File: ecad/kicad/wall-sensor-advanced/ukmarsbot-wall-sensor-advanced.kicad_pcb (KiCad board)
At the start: 2 copper layers, 27.3 x 80 mm, 30 parts, among them J1 Conn_01x14, Q1 TEFT4300, Q2 TEFT4300, Q3 TEFT4300, Q4 TEFT4300, Q5 BC337, Q6 BC337

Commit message: second draft wall sensor advanced
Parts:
- added C2: 330uF, 16V, Capacitor_THT:CP_Radial_D7.5mm_P2.50mm, F.Cu at (157.1, 129.8)
- moved C1 25.2 mm to (157.1, 80.2)
- moved D5 24.4 mm to (162.2, 106.3), turned to 90 degrees
- moved R12 20.0 mm to (158.3, 101.2), turned to -90 degrees
- moved R11 6.53 mm to (153.9, 86.6), turned to 180 degrees
- moved R1 2.92 mm to (146.3, 89.5)
- moved R4 2.92 mm to (146.3, 98.8)
- moved R5 2.92 mm to (146.3, 101.8)
- moved R6 2.92 mm to (146.3, 104.9)
- moved R7 2.92 mm to (146.3, 107.9)
- moved R13 2.92 mm to (146.3, 114.0)
- moved R14 2.92 mm to (146.3, 117.1)
- moved R2 2.92 mm to (146.3, 92.7)
- moved R3 2.92 mm to (146.3, 95.7)
- moved R8 2.92 mm to (146.3, 111.0)
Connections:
- net Net-(D1-Pad1) renamed /FWD_COMMON
- net Net-(D2-Pad1) renamed /DIA_COMMON
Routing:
- net D6_LED: track 0.00 -> 51.6 mm, vias 0 -> 4
- net A0_LF: track 5.18 -> 49.4 mm
- net A3_LF: track 4.55 -> 37.8 mm
- net A1_RD: track 4.97 -> 35.5 mm, vias 0 -> 1
- net Net-(D3-Pad2): track 0.00 -> 30.2 mm
- net A2_LD: track 4.76 -> 32.3 mm, vias 0 -> 1
- net Net-(D5-Pad2): track 20.8 -> 4.86 mm
- net 5V: track 136.8 -> 152.1 mm
- net Net-(D2-Pad2): track 0.00 -> 11.7 mm, vias 0 -> 1
- net /FWD_COMMON: track 120.8 -> 109.7 mm, vias 0 -> 1
- net V_LED: track 28.6 -> 20.0 mm
- net Net-(D4-Pad2): track 41.8 -> 38.4 mm
- net Net-(Q5-Pad2): track 32.9 -> 34.9 mm, vias 0 -> 2
- net D12_DIAGONAL: track 5.60 -> 7.56 mm
- net D11_FRONT: track 5.39 -> 7.05 mm
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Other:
- rule pad_to_mask_clearance: 0.0508 -> 0

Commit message: Update Advanced Wall Sensor
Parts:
- C1, C2: footprint Capacitor_THT:CP_Radial_D7.5mm_P2.50mm -> Capacitor_THT:CP_Radial_D10.0mm_P2.50mm
- D1, D2, D3, D4: footprint LED_THT:LED_D5.0mm_Horizontal_O3.81mm_Z3.0mm -> ukmarsbot:LED_D5.0mm_Horizontal_O6.35mm_Z3.0mm
- J1: footprint Connector_PinSocket_2.54mm:PinSocket_1x14_P2.54mm_Vertical -> ukmarsbot:PinHeader_1x14_P2.54mm_Vertical_Longpads
- Q1, Q2, Q3, Q4: footprint LED_THT:LED_D5.0mm_Horizontal_O1.27mm_Z3.0mm_IRGrey -> ukmarsbot:LED_D5.0mm_Horizontal_O1.27mm_Z3.0mm_IRGrey
- moved D4 2.07 mm to (143.8, 137.9)
- moved Q4 2.07 mm to (147.8, 136.0)
- moved D1 2.02 mm to (144.3, 74.6)
- moved Q1 2.02 mm to (147.4, 71.5)
- moved R1 0.13 mm to (146.3, 89.6)
- renumbered REF** to locked
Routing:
- net D6_LED: track 51.6 -> 21.4 mm, vias 4 -> 2
- net /FWD_COMMON: track 109.7 -> 128.5 mm
- net A0_LF: track 49.4 -> 47.6 mm
- net Net-(D4-Pad2): track 38.4 -> 39.3 mm
- net A1_RD: track 35.5 -> 35.0 mm

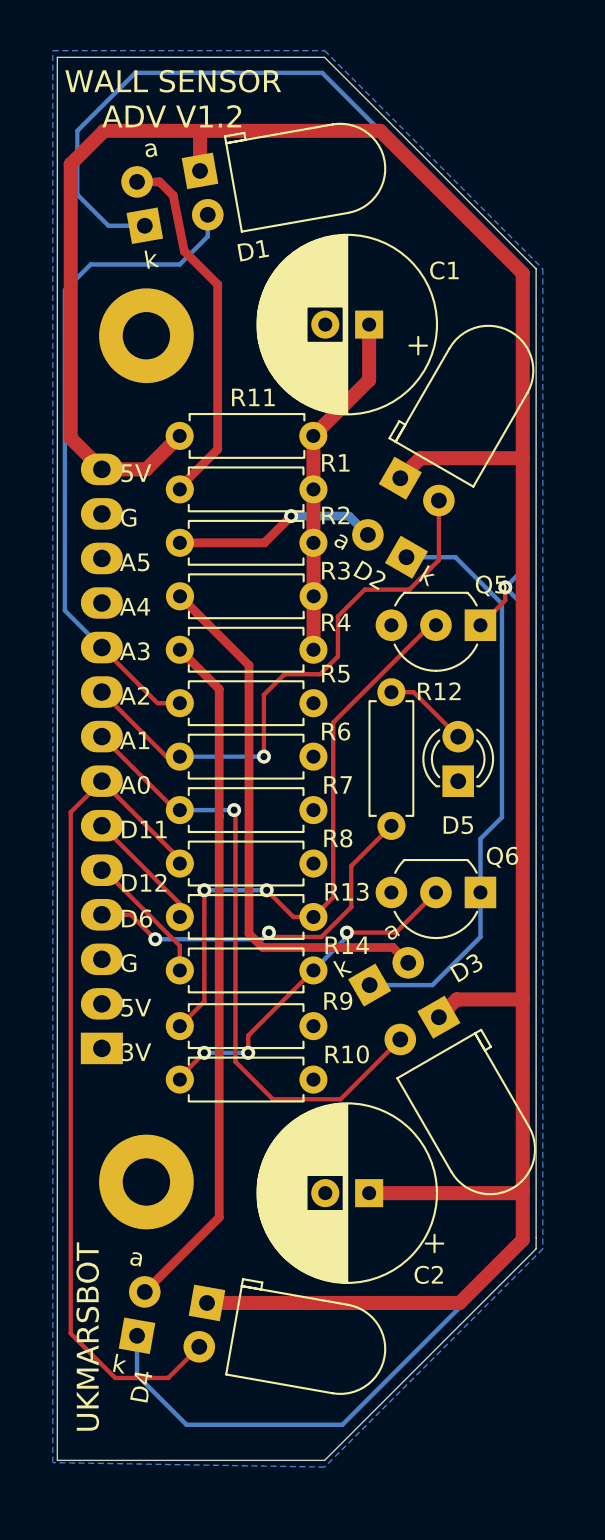
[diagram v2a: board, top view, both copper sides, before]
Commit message: use bigpad resistors on adv wall sensor
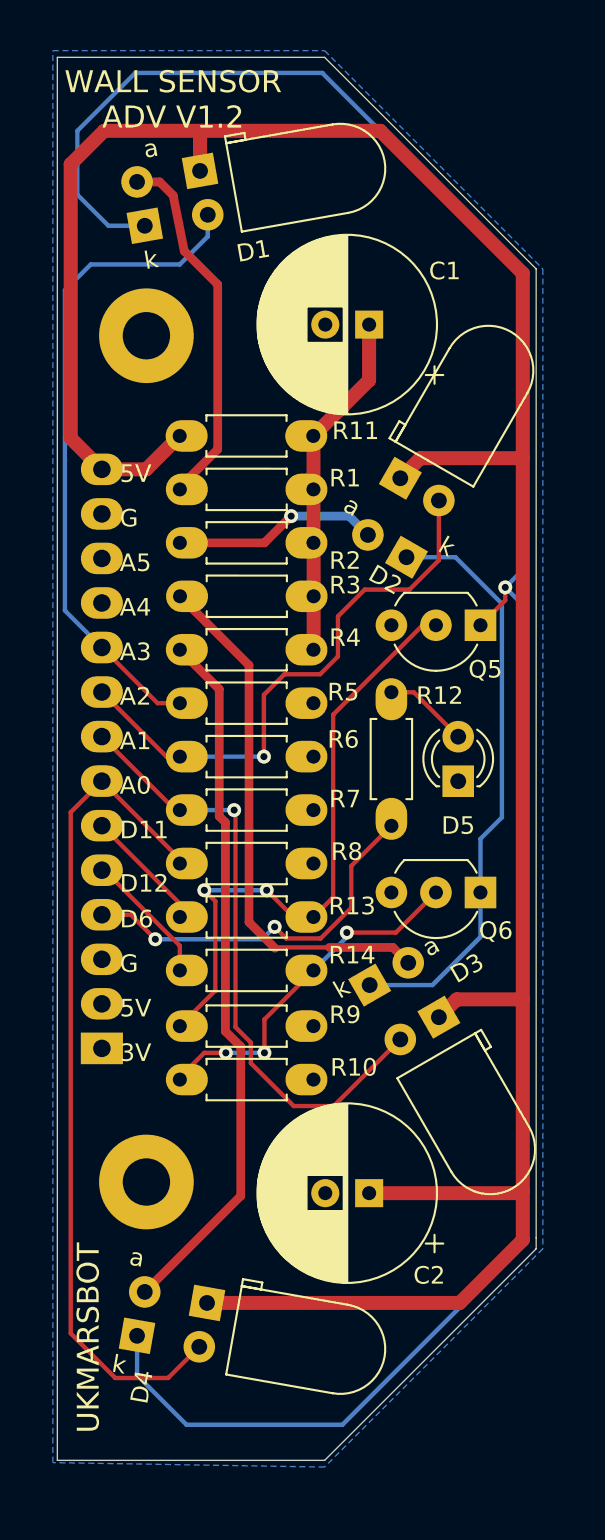
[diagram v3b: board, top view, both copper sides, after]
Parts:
- R1, R10, R11, R12, R13, R14, R2, R3, R4, R9: footprint ukmarsbot:R_Axial_DIN0207_L6.3mm_D2.5mm_P7.62mm_Horizontal -> ukmarsbot:R_Axial_DIN0207_L6.3mm_D2.5mm_P7.62mm_BIGPAD
- R5, R6, R7, R8: value 2k7 -> 1k8; footprint ukmarsbot:R_Axial_DIN0207_L6.3mm_D2.5mm_P7.62mm_Horizontal -> ukmarsbot:R_Axial_DIN0207_L6.3mm_D2.5mm_P7.62mm_BIGPAD
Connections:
- net A0_LF renamed A0_RF
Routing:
- net Net-(D4-Pad2): track 39.3 -> 40.3 mm
- net Net-(Q5-Pad2): track 34.6 -> 35.4 mm
- net Net-(Q6-Pad2): track 19.7 -> 20.2 mm

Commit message: update mounting holes on adv wall sensor
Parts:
- H1, H2: footprint MountingHole:MountingHole_2.7mm_Pad -> MountingHole:MountingHole_3.2mm_M3_Pad
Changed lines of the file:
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@@
   (net 22 "/DIA_COMMON")
   (net 23 "unconnected-(J1-Pad2)")
-  (footprint "MountingHole:MountingHole_2.7mm_Pad" (layer "F.Cu")
+  (footprint "MountingHole:MountingHole_3.2mm_M3_Pad" (layer "F.Cu")
     (at 144.37 129.13)
-    (descr "Mounting Hole 2.7mm")
-    (tags "mounting hole 2.7mm")
+    (descr "Mounting Hole 3.2mm, M3")
+    (tags "mounting hole 3.2mm m3")
     (property "Sheetfile" "ukmarsbot-wall-sensor-advanced.kicad_sch")
     (property "Sheetname" "")
     (attr exclude_from_pos_files)
-    (fp_text reference "H2" (at 0 0) (layer "F.SilkS") hide
-      (effects (font (size 1 1) (thickness 0.15)))
-    )
-    (fp_text value "3.2mm" (at 0 3.7) (layer "F.Fab")
-      (effects (font (size 1 1) (thickness 0.15)))
-    )
-    (fp_text user "${REFERENCE}" (at 0.3 0) (layer "F.Fab")
-      (effects (font (size 1 1) (thickness 0.15)))
-    )
-    (fp_circle (center 0 0) (end 2.7 0) (layer "Cmts.User") (width 0.15) (fill none))
-    (fp_circle (center 0 0) (end 2.95 0) (layer "F.CrtYd") (width 0.05) (fill none))
-    (pad "1" thru_hole circle (at 0 0) (size 5.4 5.4) (drill 2.7) (layers *.Cu *.Mask)
+    (fp_text reference "H2" (at 0 -4.2) (layer "F.SilkS")
+      (effects (font (size 1 1) (thickness 0.15)))
+    )
+    (fp_text value "3.2mm" (at 0 4.2) (layer "F.Fab")
+      (effects (font (size 1 1) (thickness 0.15)))
+    )
+    (fp_text user "${REFERENCE}" (at 0 0) (layer "F.Fab")
+      (effects (font (size 1 1) (thickness 0.15)))
+    )
+    (fp_circle (center 0 0) (end 3.2 0) (layer "Cmts.User") (width 0.15) (fill none))
+    (fp_circle (center 0 0) (end 3.45 0) (layer "F.CrtYd") (width 0.05) (fill none))
+    (pad "1" thru_hole circle (at 0 0) (size 6.4 6.4) (drill 3.2) (layers *.Cu *.Mask)
       (net 3 "GND") (pinfunction "1") (pintype "input"))
   )
@@
     )
   )
-  (footprint "MountingHole:MountingHole_2.7mm_Pad" (layer "F.Cu")
+  (footprint "MountingHole:MountingHole_3.2mm_M3_Pad" (layer "F.Cu")
     (at 144.37 80.87)
-    (descr "Mounting Hole 2.7mm")
-    (tags "mounting hole 2.7mm")
+    (descr "Mounting Hole 3.2mm, M3")
+    (tags "mounting hole 3.2mm m3")
     (property "Sheetfile" "ukmarsbot-wall-sensor-advanced.kicad_sch")
     (property "Sheetname" "")
     (attr exclude_from_pos_files)
-    (fp_text reference "H1" (at 0 0) (layer "F.SilkS") hide
-      (effects (font (size 1 1) (thickness 0.15)))
-    )
-    (fp_text value "3.2mm" (at 0 3.7) (layer "F.Fab")
-      (effects (font (size 1 1) (thickness 0.15)))
-    )
-    (fp_text user "${REFERENCE}" (at 0.3 0) (layer "F.Fab")
-      (effects (font (size 1 1) (thickness 0.15)))
-    )
-    (fp_circle (center 0 0) (end 2.7 0) (layer "Cmts.User") (width 0.15) (fill none))
-    (fp_circle (center 0 0) (end 2.95 0) (layer "F.CrtYd") (width 0.05) (fill none))
-    (pad "1" thru_hole circle (at 0 0) (size 5.4 5.4) (drill 2.7) (layers *.Cu *.Mask)
+    (fp_text reference "H1" (at 0 -4.2) (layer "F.SilkS")
+      (effects (font (size 1 1) (thickness 0.15)))
+    )
+    (fp_text value "3.2mm" (at 0 4.2) (layer "F.Fab")
+      (effects (font (size 1 1) (thickness 0.15)))
+    )
+    (fp_text user "${REFERENCE}" (at 0 0) (layer "F.Fab")
+      (effects (font (size 1 1) (thickness 0.15)))
+    )
+    (fp_circle (center 0 0) (end 3.2 0) (layer "Cmts.User") (width 0.15) (fill none))
+    (fp_circle (center 0 0) (end 3.45 0) (layer "F.CrtYd") (width 0.05) (fill none))
+    (pad "1" thru_hole circle (at 0 0) (size 6.4 6.4) (drill 3.2) (layers *.Cu *.Mask)
       (net 3 "GND") (pinfunction "1") (pintype "input"))
   )

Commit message: re-route and update adv wall sensor
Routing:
- net Net-(D3-Pad2): track 30.3 -> 35.7 mm, vias 0 -> 2
- net A2_LD: track 32.2 -> 33.8 mm
- net A1_RD: track 34.8 -> 35.9 mm
- net A0_RF: track 47.6 -> 48.6 mm
- net A3_LF: track 37.7 -> 36.7 mm
- net /DIA_COMMON: track 33.5 -> 34.3 mm
- net Net-(D4-Pad2): track 40.3 -> 39.7 mm
- net Net-(Q6-Pad2): track 20.2 -> 19.9 mm, vias 3 -> 2

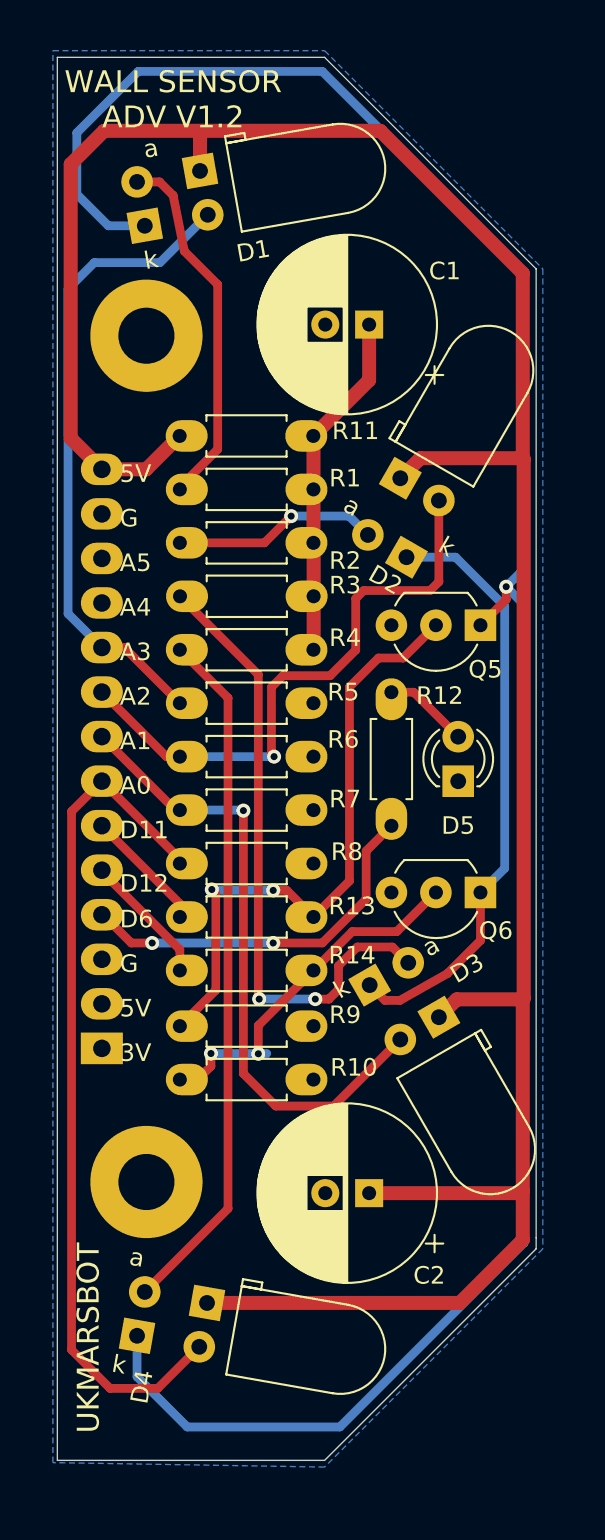
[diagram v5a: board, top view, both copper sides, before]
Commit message: update emitter values in advanced wall sensor
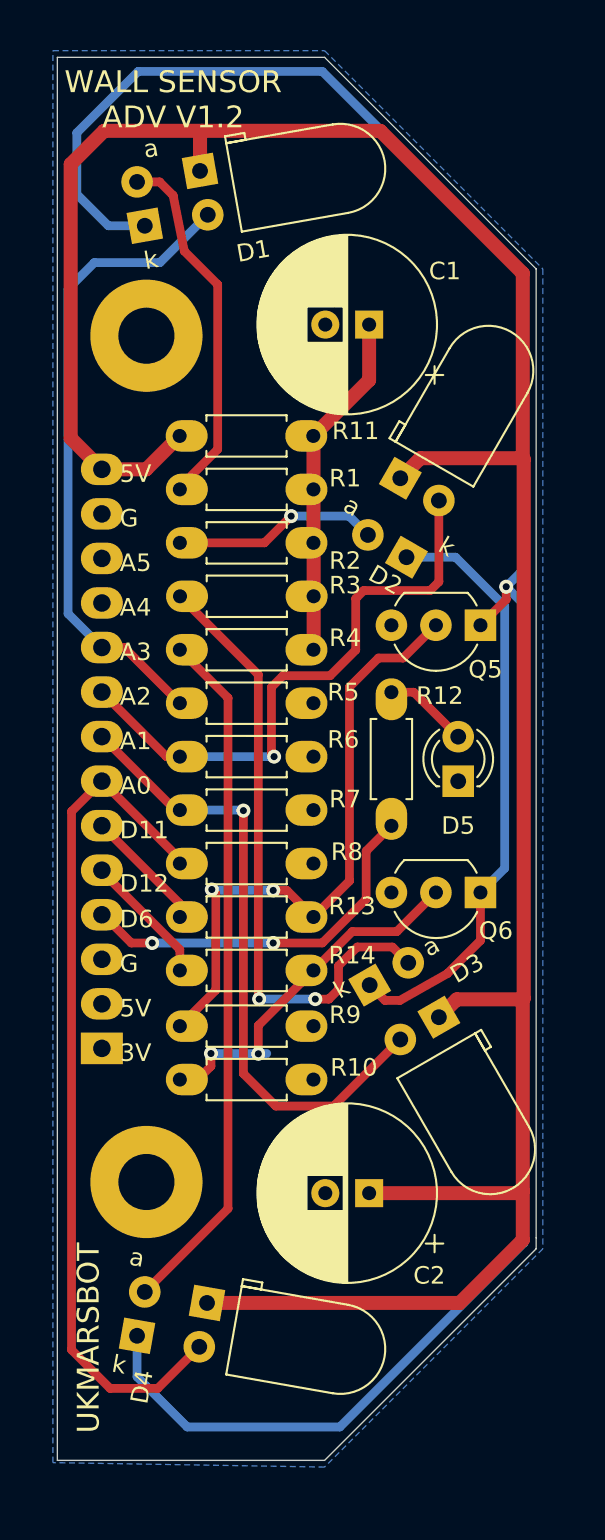
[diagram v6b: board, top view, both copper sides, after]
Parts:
- D1, D2, D3, D4: value SFH4550 -> SFH4545
- renumbered locked to REF**
